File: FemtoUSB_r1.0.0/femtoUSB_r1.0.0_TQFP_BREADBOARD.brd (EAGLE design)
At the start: 40.6 x 19.1 mm, 27 parts, among them IC1 ATSAMD21E18A-AU

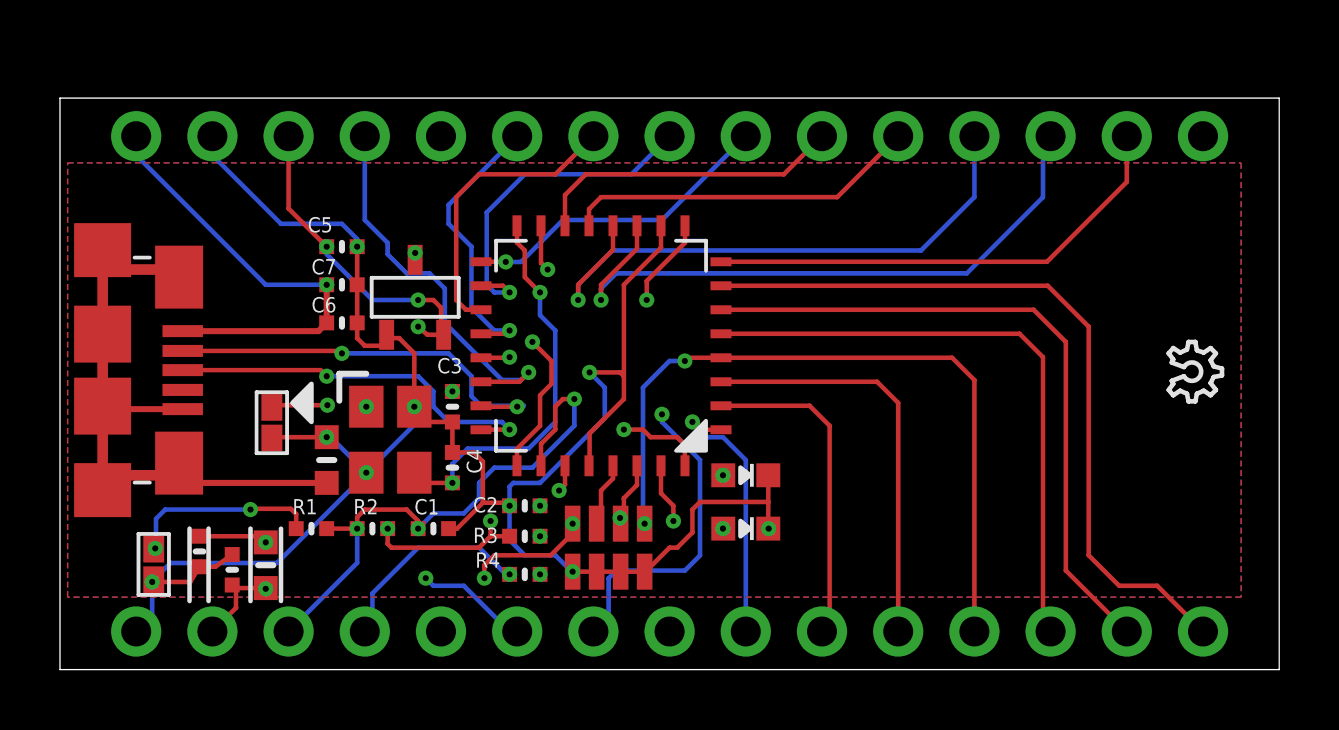
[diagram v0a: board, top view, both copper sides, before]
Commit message: Updating gerbers and BoM/Partslist of QFN version
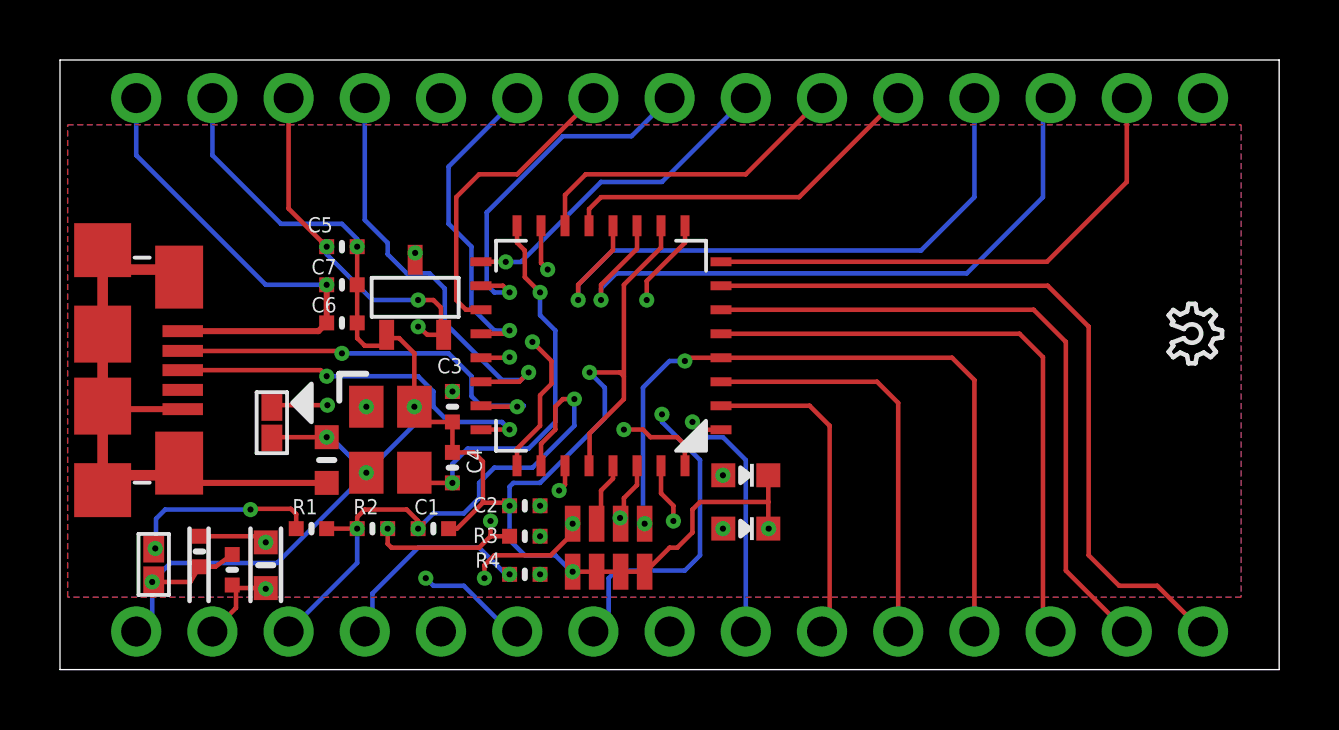
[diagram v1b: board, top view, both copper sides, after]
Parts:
- EPSON_TSX1: value 32MHz -> 48MHz
- moved PINS_LEFT 1.27 mm to (20.3, 19.1)
- moved U$35 1.27 mm to (37.0, 12.2)
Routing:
- net PA09/I2S/MCK0/I2C: track 19.9 -> 21.2 mm
- net PA08/I2S/SD1/I2C: track 21.5 -> 22.8 mm
- net PA07/AIN[7]/I2S/SD[0]: track 16.2 -> 17.4 mm
- net VIN: track 19.0 -> 20.2 mm
- net PA23/USB/SOF1KHZ/I2C: track 13.2 -> 14.4 mm
- net PA22/I2C: track 9.57 -> 10.8 mm
- net PA19/SERCOM1/PAD[3]/SPI: track 9.56 -> 10.8 mm
- net GND: track 72.5 -> 73.7 mm
- net 3.3V: track 41.8 -> 43.1 mm
- net PA17/SERCOM1/PAD[1]/SPI/I2C: track 11.5 -> 12.0 mm
- net PA16/SERCOM1/PAD[0]/SPI/I2C: track 10.6 -> 11.1 mm
- net PA11/I2S/FS0: track 10.4 -> 10.9 mm
- net PA18/SERCOM1/PAD[2]/SPI: track 9.80 -> 10.3 mm
- net PA10/I2S/SCK0: track 11.9 -> 12.4 mm
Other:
- board size 40.6 x 19.1 mm -> 40.6 x 20.3 mm
- board text added: "r1.0.3 TQFP"
- board text removed: "r1.0.2 TQFP"
